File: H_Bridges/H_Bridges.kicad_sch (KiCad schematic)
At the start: 28 parts, among them J1 S4B-PH-K-SLFSN, Q1 IRF540NSTRLPBF, Q2 IRF540NSTRLPBF, Q3 IRF540NSTRLPBF, Q4 IRF540NSTRLPBF, Q5 IRF540NSTRLPBF, Q6 IRF540NSTRLPBF, Q7 IRF540NSTRLPBF, Q8 IRF540NSTRLPBF, U1 ESP8266

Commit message: added resistor footprints
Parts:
- R1, R10, R2, R3, R4, R5, R6, R7, R8, R9: footprint (none) -> Resistor_SMD:R_0603_1608Metric
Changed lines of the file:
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@@
 			)
 		)
-		(property "Footprint" ""
+		(property "Footprint" "Resistor_SMD:R_0603_1608Metric"
 			(at 113.284 31.496 90)
 			(effects
@@
 			)
 		)
-		(property "Footprint" ""
+		(property "Footprint" "Resistor_SMD:R_0603_1608Metric"
 			(at 191.516 46.736 90)
 			(effects
@@
 			)
 		)
-		(property "Footprint" ""
+		(property "Footprint" "Resistor_SMD:R_0603_1608Metric"
 			(at 30.734 75.184 90)
 			(effects
@@
 			)
 		)
-		(property "Footprint" ""
+		(property "Footprint" "Resistor_SMD:R_0603_1608Metric"
 			(at 33.274 169.164 90)
 			(effects
@@
 			)
 		)
-		(property "Footprint" ""
+		(property "Footprint" "Resistor_SMD:R_0603_1608Metric"
 			(at 30.734 49.784 90)
 			(effects
@@
 			)
 		)
-		(property "Footprint" ""
+		(property "Footprint" "Resistor_SMD:R_0603_1608Metric"
 			(at 115.824 125.476 90)
 			(effects
@@
 			)
 		)
-		(property "Footprint" ""
+		(property "Footprint" "Resistor_SMD:R_0603_1608Metric"
 			(at 115.824 187.706 90)
 			(effects
@@
 			)
 		)
-		(property "Footprint" ""
+		(property "Footprint" "Resistor_SMD:R_0603_1608Metric"
 			(at 33.274 143.764 90)
 			(effects
@@
 			)
 		)
-		(property "Footprint" ""
+		(property "Footprint" "Resistor_SMD:R_0603_1608Metric"
 			(at 191.516 49.276 90)
 			(effects
@@
 			)
 		)
-		(property "Footprint" ""
+		(property "Footprint" "Resistor_SMD:R_0603_1608Metric"
 			(at 113.284 93.726 90)
 			(effects

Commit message: finished component placement
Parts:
- removed R10, R9: 0, Resistor_SMD:R_0603_1608Metric, symbol Device:R_US
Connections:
- net +5V: now also U1.9 (VBAT)
- net P3: now also U1.17 (GPIO4); no longer U1.6 (GPIO12)
- net P4: now also U1.16 (GPIO0); no longer U1.7 (GPIO13)
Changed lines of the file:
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@@
 	)
 	(junction
-		(at 182.88 45.72)
-		(diameter 0)
-		(color 0 0 0 0)
-	)
-	(junction
 		(at 97.79 40.64)
 		(diameter 0)
@@
 	(wire
 		(pts
-			(xy 195.58 45.72) (xy 219.71 45.72)
-		)
-		(stroke
-			(width 0)
-			(type default)
-		)
-	)
-	(wire
-		(pts
 			(xy 116.84 50.8) (xy 114.3 50.8)
 		)
@@
 	(wire
 		(pts
-			(xy 195.58 48.26) (xy 219.71 48.26)
-		)
-		(stroke
-			(width 0)
-			(type default)
-		)
-	)
-	(wire
-		(pts
 			(xy 78.74 40.64) (xy 50.8 40.64)
 		)
@@
 	(wire
 		(pts
-			(xy 182.88 48.26) (xy 182.88 45.72)
+			(xy 182.88 40.64) (xy 182.88 48.26)
 		)
 		(stroke
@@
 	(wire
 		(pts
-			(xy 127 149.86) (xy 127 157.48)
+			(xy 257.81 38.1) (xy 257.81 33.02)
 		)
 		(stroke
@@
 	(wire
 		(pts
-			(xy 116.84 184.15) (xy 116.84 168.91)
+			(xy 127 149.86) (xy 127 157.48)
 		)
 		(stroke
@@
 	(wire
 		(pts
-			(xy 127 157.48) (xy 127 163.83)
+			(xy 116.84 184.15) (xy 116.84 168.91)
 		)
 		(stroke
@@
 	(wire
 		(pts
-			(xy 87.63 34.29) (xy 87.63 40.64)
+			(xy 127 157.48) (xy 127 163.83)
 		)
 		(stroke
@@
 	(wire
 		(pts
-			(xy 204.47 40.64) (xy 204.47 33.02)
+			(xy 87.63 34.29) (xy 87.63 40.64)
 		)
 		(stroke
@@
 	(wire
 		(pts
+			(xy 254 35.56) (xy 246.38 35.56)
+		)
+		(stroke
+			(width 0)
+			(type default)
+		)
+	)
+	(wire
+		(pts
 			(xy 114.3 22.86) (xy 114.3 27.94)
 		)
@@
 	(wire
 		(pts
-			(xy 246.38 45.72) (xy 254 45.72)
+			(xy 246.38 45.72) (xy 273.05 45.72)
 		)
 		(stroke
@@
 	(wire
 		(pts
-			(xy 187.96 48.26) (xy 182.88 48.26)
+			(xy 182.88 48.26) (xy 219.71 48.26)
 		)
 		(stroke
@@
 	(wire
 		(pts
-			(xy 254 45.72) (xy 254 43.18)
+			(xy 273.05 45.72) (xy 273.05 43.18)
 		)
 		(stroke
@@
 	(wire
 		(pts
-			(xy 200.66 43.18) (xy 200.66 33.02)
-		)
-		(stroke
-			(width 0)
-			(type default)
-		)
-	)
-	(wire
-		(pts
 			(xy 88.9 134.62) (xy 81.28 134.62)
 		)
@@
 	(wire
 		(pts
-			(xy 187.96 45.72) (xy 182.88 45.72)
-		)
-		(stroke
-			(width 0)
-			(type default)
-		)
-	)
-	(wire
-		(pts
 			(xy 217.17 50.8) (xy 219.71 50.8)
 		)
@@
 	(wire
 		(pts
-			(xy 219.71 43.18) (xy 200.66 43.18)
+			(xy 114.3 90.17) (xy 114.3 74.93)
 		)
 		(stroke
@@
 	(wire
 		(pts
-			(xy 114.3 90.17) (xy 114.3 74.93)
+			(xy 114.3 74.93) (xy 116.84 74.93)
 		)
 		(stroke
@@
 	(wire
 		(pts
-			(xy 114.3 74.93) (xy 116.84 74.93)
+			(xy 218.44 86.36) (xy 236.22 86.36)
 		)
 		(stroke
@@
 	(wire
 		(pts
-			(xy 218.44 86.36) (xy 236.22 86.36)
+			(xy 100.33 171.45) (xy 100.33 179.07)
 		)
 		(stroke
@@
 	(wire
 		(pts
-			(xy 100.33 171.45) (xy 100.33 179.07)
+			(xy 81.28 148.59) (xy 81.28 157.48)
 		)
 		(stroke
@@
 	(wire
 		(pts
-			(xy 81.28 148.59) (xy 81.28 157.48)
+			(xy 81.28 171.45) (xy 81.28 179.07)
 		)
 		(stroke
@@
 	(wire
 		(pts
-			(xy 81.28 171.45) (xy 81.28 179.07)
+			(xy 254 33.02) (xy 254 35.56)
 		)
 		(stroke
@@
 	(wire
 		(pts
-			(xy 182.88 40.64) (xy 182.88 45.72)
-		)
-		(stroke
-			(width 0)
-			(type default)
-		)
-	)
-	(wire
-		(pts
 			(xy 88.9 128.27) (xy 88.9 134.62)
 		)
@@
 	(wire
 		(pts
+			(xy 246.38 38.1) (xy 257.81 38.1)
+		)
+		(stroke
+			(width 0)
+			(type default)
+		)
+	)
+	(wire
+		(pts
 			(xy 34.29 50.8) (xy 43.18 50.8)
 		)
@@
 	(wire
 		(pts
-			(xy 219.71 40.64) (xy 204.47 40.64)
-		)
-		(stroke
-			(width 0)
-			(type default)
-		)
-	)
-	(wire
-		(pts
 			(xy 219.71 38.1) (xy 208.28 38.1)
 		)
@@
 	)
 	(label "P3"
-		(at 204.47 33.02 0)
+		(at 254 33.02 0)
 		(fields_autoplaced yes)
 		(effects
@@
 	)
 	(label "P4"
-		(at 200.66 33.02 0)
+		(at 257.81 33.02 0)
 		(fields_autoplaced yes)
 		(effects
@@
 	(symbol
 		(lib_id "Device:R_US")
-		(at 191.77 45.72 270)
-		(unit 1)
-		(exclude_from_sim no)
-		(in_bom yes)
-		(on_board yes)
-		(dnp no)
-		(property "Reference" "R9"
-			(at 189.23 43.688 90)
-			(effects
-				(font
-					(size 1.27 1.27)
-				)
-			)
-		)
-		(property "Value" "0"
-			(at 193.802 43.688 90)
-			(effects
-				(font
-					(size 1.27 1.27)
-				)
-			)
-		)
-		(property "Footprint" "Resistor_SMD:R_0603_1608Metric"
-			(at 191.516 46.736 90)
-			(effects
-				(font
-					(size 1.27 1.27)
-				)
-				(hide yes)
-			)
-		)
-		(property "Datasheet" "~"
-			(at 191.77 45.72 0)
-			(effects
-				(font
-					(size 1.27 1.27)
-				)
-				(hide yes)
-			)
-		)
-		(property "Description" "Resistor, US symbol"
-			(at 191.77 45.72 0)
-			(effects
-				(font
-					(size 1.27 1.27)
-				)
-				(hide yes)
-			)
-		)
-		(pin "2"
-		)
-		(pin "1"
-		)
-		(instances
-			(project "H_Bridges"
-				(path "/a020a591-cea5-4f16-9764-82374c05e734"
-					(reference "R9")
-					(unit 1)
-				)
-			)
-		)
-	)
-	(symbol
-		(lib_id "Device:R_US")
 		(at 30.48 76.2 90)
 		(unit 1)
@@
 	(symbol
 		(lib_id "power:+3V3")
-		(at 254 43.18 0)
+		(at 273.05 43.18 0)
 		(unit 1)
 		(exclude_from_sim no)
@@
 		(fields_autoplaced yes)
 		(property "Reference" "#PWR08"
-			(at 254 46.99 0)
+			(at 273.05 46.99 0)
 			(effects
 				(font
@@
 		)
 		(property "Value" "+3V3"
-			(at 254 38.1 0)
+			(at 273.05 38.1 0)
 			(effects
 				(font
@@
 		)
 		(property "Footprint" ""
-			(at 254 43.18 0)
+			(at 273.05 43.18 0)
 			(effects
 				(font
@@
 		)
 		(property "Datasheet" ""
-			(at 254 43.18 0)
+			(at 273.05 43.18 0)
 			(effects
 				(font
@@
 		)
 		(property "Description" "Power symbol creates a global label with name \"+3V3\""
-			(at 254 43.18 0)
+			(at 273.05 43.18 0)
 			(effects
 				(font
@@
 					(unit 1)
 				)
-			)
-		)
-	)
-	(symbol
-		(lib_id "Device:R_US")
-		(at 191.77 48.26 270)
-		(unit 1)
-		(exclude_from_sim no)
-		(in_bom yes)
-		(on_board yes)
-		(dnp no)
-		(property "Reference" "R10"
-			(at 189.23 50.292 90)
-			(effects
-				(font
-					(size 1.27 1.27)
-				)
-			)
-		)
-		(property "Value" "0"
-			(at 193.548 50.292 90)
-			(effects
-				(font
-					(size 1.27 1.27)
-				)
-			)
-		)
-		(property "Footprint" "Resistor_SMD:R_0603_1608Metric"
-			(at 191.516 49.276 90)
-			(effects
-				(font
-					(size 1.27 1.27)
-				)
-				(hide yes)
-			)
-		)
-		(property "Datasheet" "~"
-			(at 191.77 48.26 0)
-			(effects
-				(font
-					(size 1.27 1.27)
-				)
-				(hide yes)
-			)
-		)
-		(property "Description" "Resistor, US symbol"
-			(at 191.77 48.26 0)
-			(effects
-				(font
-					(size 1.27 1.27)
-				)
-				(hide yes)
-			)
-		)
-		(pin "2"
-		)
-		(pin "1"
-		)
-		(instances
-			(project "H_Bridges"
-				(path "/a020a591-cea5-4f16-9764-82374c05e734"
-					(reference "R10")
-					(unit 1)
-				)

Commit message: routing start
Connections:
- net P3: now also U1.6 (GPIO12); no longer U1.17 (GPIO4)
- net P4: now also U1.7 (GPIO13); no longer U1.16 (GPIO0)
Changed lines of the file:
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@@
+	(wire
+		(pts
+			(xy 196.85 43.18) (xy 219.71 43.18)
+		)
+		(stroke
+			(width 0)
+			(type default)
+		)
+	)
 	(wire
 		(pts
@@
 	(wire
 		(pts
-			(xy 257.81 38.1) (xy 257.81 33.02)
-		)
-		(stroke
-			(width 0)
-			(type default)
-		)
-	)
-	(wire
-		(pts
 			(xy 127 149.86) (xy 127 157.48)
 		)
@@
 	(wire
 		(pts
-			(xy 254 35.56) (xy 246.38 35.56)
-		)
-		(stroke
-			(width 0)
-			(type default)
-		)
-	)
-	(wire
-		(pts
 			(xy 114.3 22.86) (xy 114.3 27.94)
 		)
@@
 	(wire
 		(pts
-			(xy 254 33.02) (xy 254 35.56)
-		)
-		(stroke
-			(width 0)
-			(type default)
-		)
-	)
-	(wire
-		(pts
 			(xy 124.46 55.88) (xy 124.46 63.5)
 		)
@@
 	(wire
 		(pts
+			(xy 200.66 40.64) (xy 219.71 40.64)
+		)
+		(stroke
+			(width 0)
+			(type default)
+		)
+	)
+	(wire
+		(pts
 			(xy 124.46 63.5) (xy 124.46 69.85)
 		)
@@
 	(wire
 		(pts
-			(xy 246.38 38.1) (xy 257.81 38.1)
-		)
-		(stroke
-			(width 0)
-			(type default)
-		)
-	)
-	(wire
-		(pts
 			(xy 34.29 50.8) (xy 43.18 50.8)
 		)
@@
 	(wire
 		(pts
+			(xy 200.66 38.1) (xy 200.66 40.64)
+		)
+		(stroke
+			(width 0)
+			(type default)
+		)
+	)
+	(wire
+		(pts
 			(xy 124.46 101.6) (xy 114.3 101.6)
 		)
@@
 	(wire
 		(pts
+			(xy 196.85 43.18) (xy 196.85 38.1)
+		)
+		(stroke
+			(width 0)
+			(type default)
+		)
+	)
+	(wire
+		(pts
 			(xy 87.63 85.09) (xy 87.63 87.63)
 		)
@@
 			(width 0)
 			(type default)
+		)
+	)
+	(label "P3"
+		(at 200.66 38.1 0)
+		(fields_autoplaced yes)
+		(effects
+			(font
+				(size 1.27 1.27)
+			)
+			(justify left bottom)
 		)
 	)
@@
 		)
 	)
-	(label "P3"
-		(at 254 33.02 0)
+	(label "P4"
+		(at 196.85 38.1 0)
 		(fields_autoplaced yes)
 		(effects
@@
 		(fields_autoplaced yes)
 		(effects
-			(font
-				(size 1.27 1.27)
-			)
-			(justify left bottom)
-		)
-	)
-	(label "P4"
-		(at 257.81 33.02 0)
-		(fields_autoplaced yes)
-		(effects

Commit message: finished routing
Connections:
- net P1: now also U1.5 (GPIO14); no longer U1.4 (GPIO16)
- net P2: now also U1.4 (GPIO16); no longer U1.5 (GPIO14)
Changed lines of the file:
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@@
 		)
 	)
-	(label "P1"
+	(label "P2"
 		(at 212.09 33.02 0)
 		(fields_autoplaced yes)
@@
 		)
 	)
-	(label "P2"
+	(label "P1"
 		(at 208.28 33.02 0)
 		(fields_autoplaced yes)

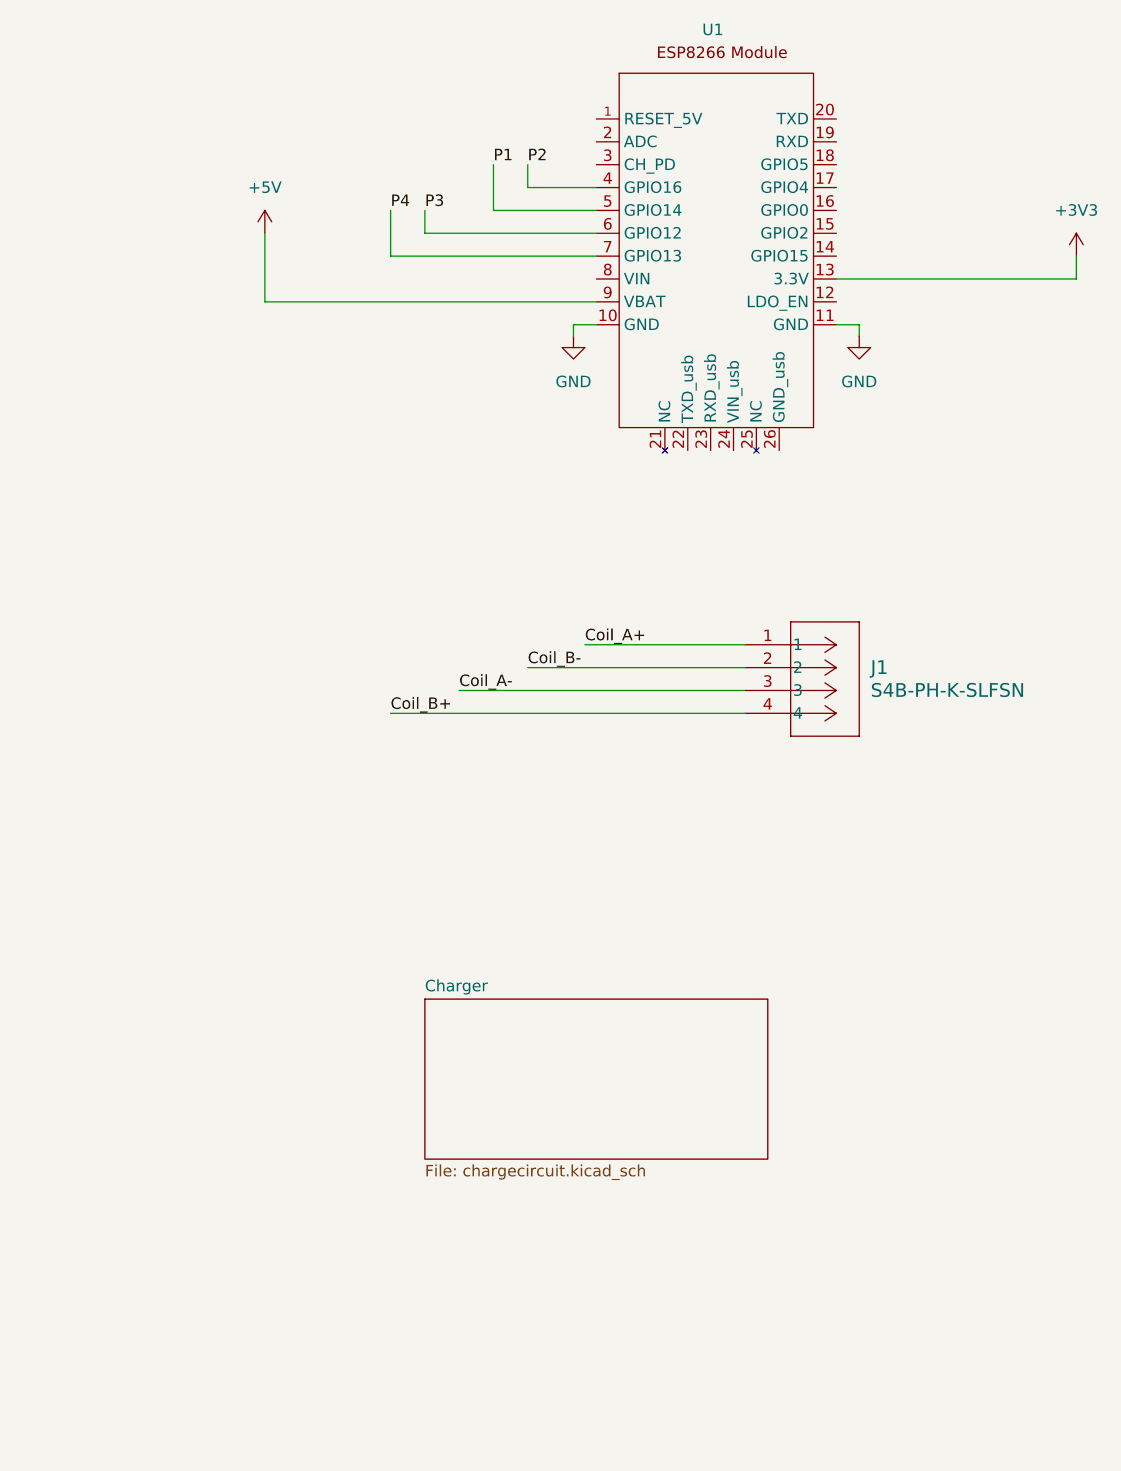
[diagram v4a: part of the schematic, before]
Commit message: added sim for H-bridge
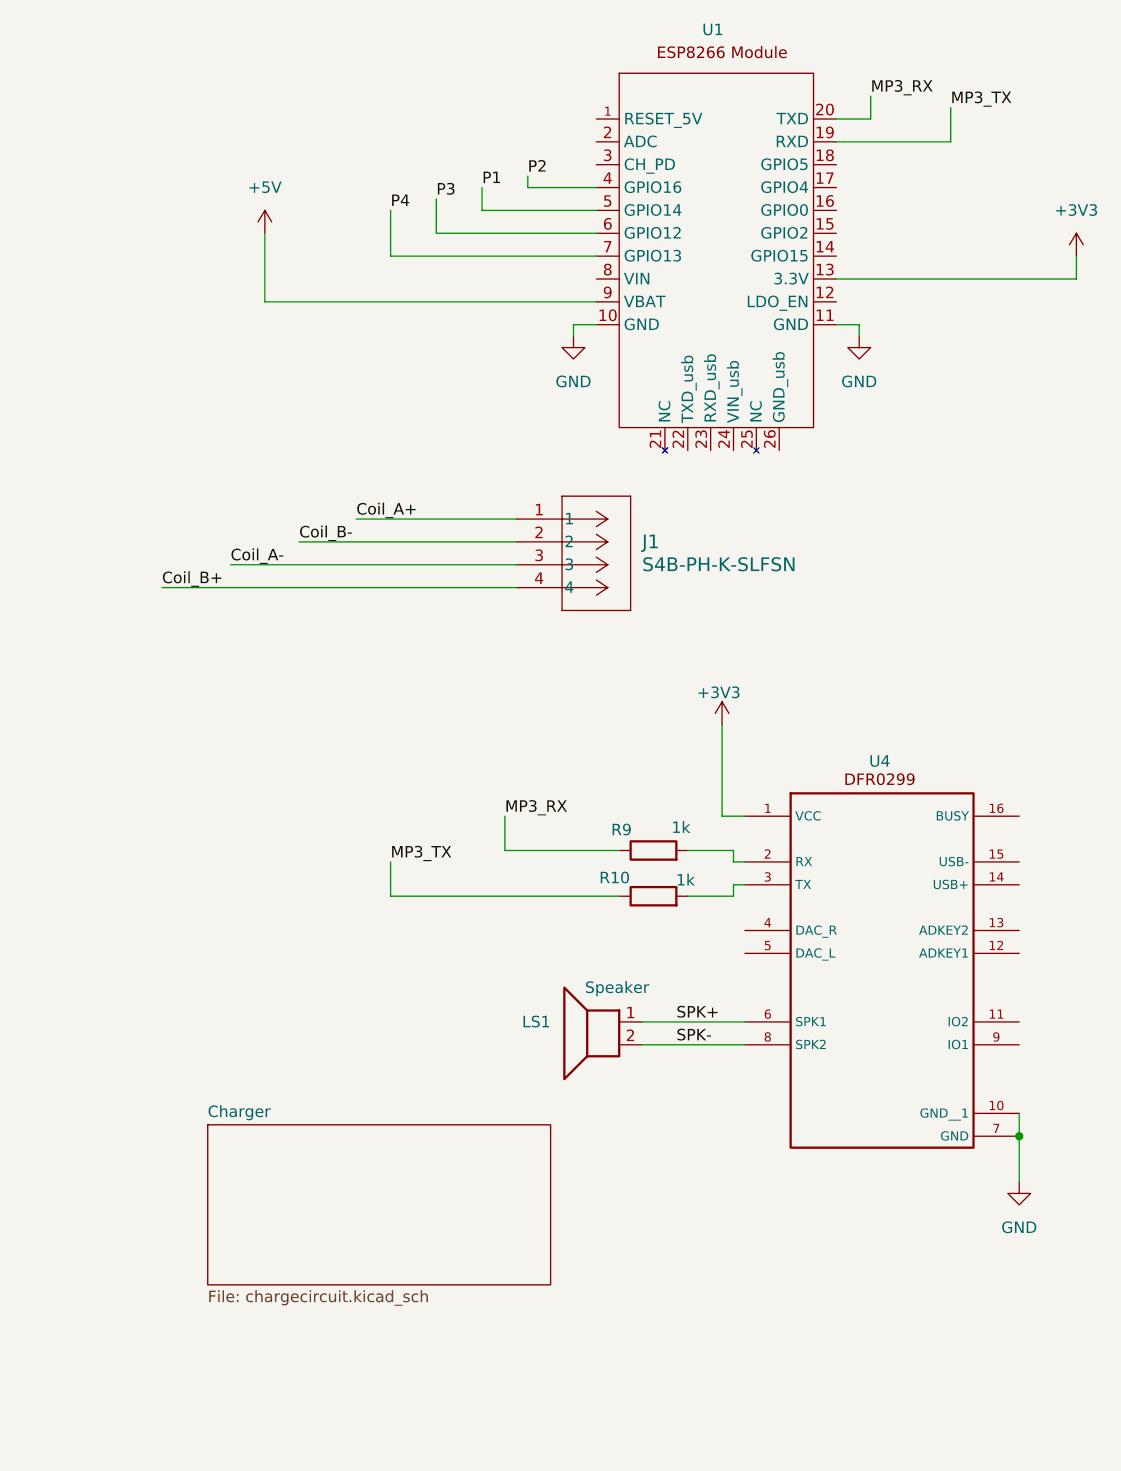
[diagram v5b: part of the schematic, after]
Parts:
- added LS1: Speaker, Footprints:Speaker, symbol Device:Speaker
- added R10, R9: 1k, Resistor_SMD:R_0402_1005Metric, symbol Device:R
- added U4: ~, Footprints:MODULE_DFR0299, symbol Detection_Eval_lib:DFR0299
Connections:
- net +3V3: now also U4.1 (VCC)
- net GND: now also U4.10 (GND__1), U4.7 (GND)
- net MP3_TX: now reaches U1.19 (RXD)
- net MP3_TX: now also R10.1
- net MP3_RX: now reaches U1.20 (TXD)
- net MP3_RX: now also R9.1
- new net: R9.2, U4.2 (RX)
- new net: R10.2, U4.3 (TX)
- new net SPK+: LS1.1, U4.6 (SPK1)
- new net SPK-: LS1.2, U4.8 (SPK2)
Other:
- moved on the sheet: J1

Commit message: made final changes
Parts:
- U1: footprint ESP8266_THT:ESP8266_THT -> Module:Adafruit_HUZZAH_ESP8266_breakout
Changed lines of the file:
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@@
 			)
 		)
-		(property "Footprint" "ESP8266_THT:ESP8266_THT"
+		(property "Footprint" "Module:Adafruit_HUZZAH_ESP8266_breakout"
 			(at 229.87 49.53 0)
 			(effects
